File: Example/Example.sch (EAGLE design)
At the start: 20 parts, among them IC1 LM555D, IC2 74LS02D, IC3 74LS02D, J1 UX60-MB-5S8, SW1 MFS101D-6-Z

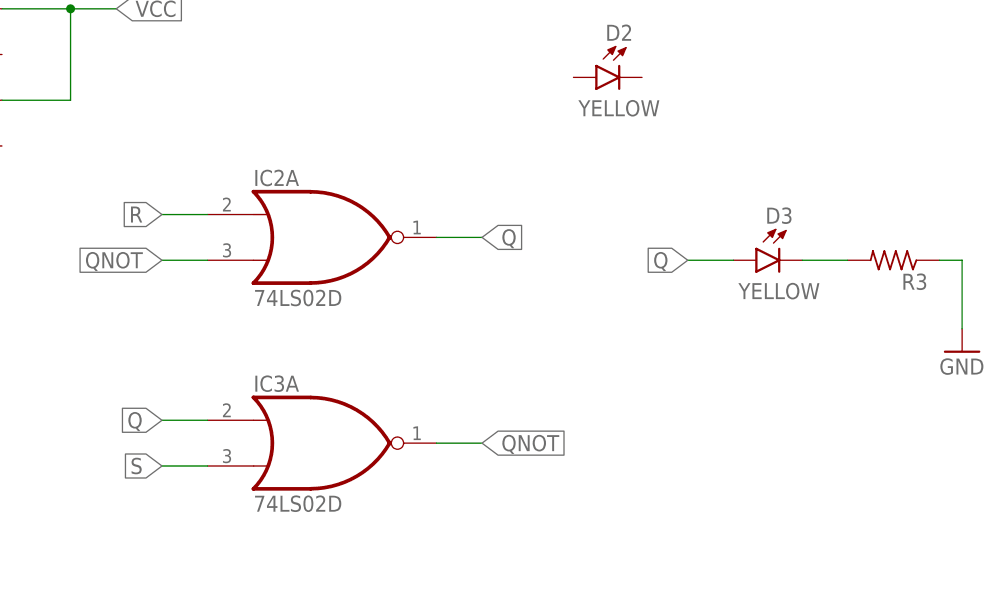
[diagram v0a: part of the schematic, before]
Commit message: Fixed issue of second NOR gate. However, did not delete second NOR gate.
I could not change the attributes of the NOR gates.
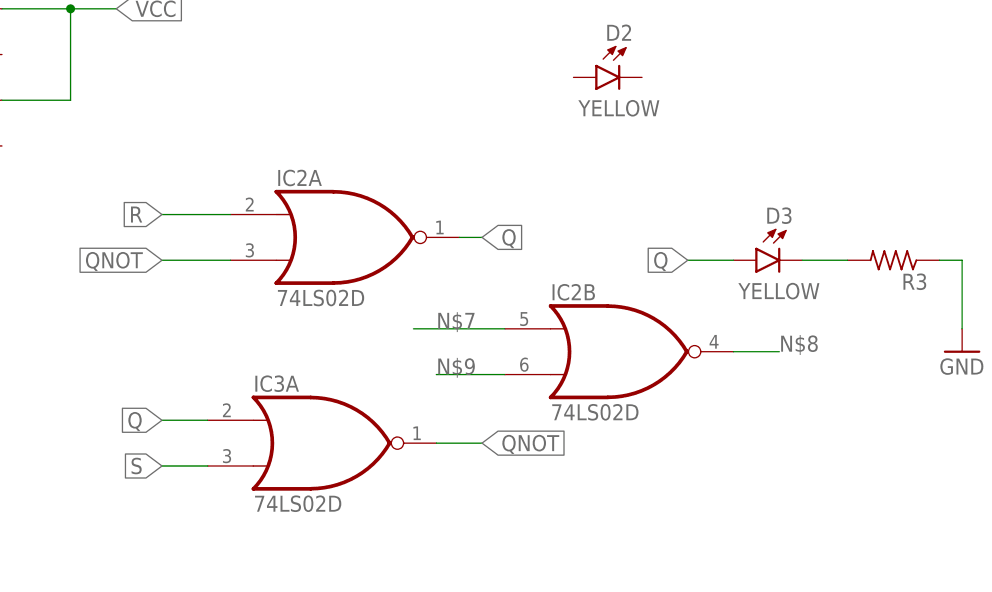
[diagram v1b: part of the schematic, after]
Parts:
- IC2: SPICEPREFIX (none) -> J
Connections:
- new net N$7: IC2B.I0
- new net N$8: IC2B.O
- new net N$9: IC2B.I1
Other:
- moved on the sheet: IC2A
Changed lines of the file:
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@@
 <?xml version="1.0" encoding="utf-8"?>
 <!DOCTYPE eagle SYSTEM "eagle.dtd">
-<eagle version="9.5.1">
+<eagle version="9.5.2">
 <drawing>
 <settings>
@@
 <part name="SUPPLY12" library="RoboJackets-Supplies" deviceset="GND" device=""/>
 <part name="SW1" library="Example" deviceset="MFS101D-6-Z" device="" override_package3d_urn="urn:adsk.eagle:package:25000897/2" override_package_urn="urn:adsk.eagle:footprint:25000899/1"/>
-<part name="IC2" library="74xx-us" library_urn="urn:adsk.eagle:library:88" deviceset="74*02" device="D" package3d_urn="urn:adsk.eagle:package:2917/1" technology="LS"/>
+<part name="IC2" library="74xx-us" library_urn="urn:adsk.eagle:library:88" deviceset="74*02" device="D" package3d_urn="urn:adsk.eagle:package:2917/1" technology="LS">
+<attribute name="SPICEPREFIX" value="J"/>
+</part>
 <part name="S1" library="adafruit" library_urn="urn:adsk.eagle:library:420" deviceset="40-XX" device="-ROUND" package3d_urn="urn:adsk.eagle:package:6240926/1"/>
 <part name="U$1" library="adafruit" library_urn="urn:adsk.eagle:library:420" deviceset="CR1220" device="SMT" package3d_urn="urn:adsk.eagle:package:6240665/1"/>
@@
 <attribute name="VALUE" x="107.696" y="154.178" size="1.778" layer="96" rot="R180"/>
 </instance>
-<instance part="IC2" gate="A" x="195.58" y="88.9" smashed="yes">
-<attribute name="NAME" x="187.96" y="94.615" size="1.778" layer="95"/>
-<attribute name="VALUE" x="187.96" y="81.28" size="1.778" layer="96"/>
+<instance part="IC2" gate="A" x="198.12" y="88.9" smashed="yes">
+<attribute name="NAME" x="190.5" y="94.615" size="1.778" layer="95"/>
+<attribute name="VALUE" x="190.5" y="81.28" size="1.778" layer="96"/>
 </instance>
 <instance part="S1" gate="1" x="127" y="88.9" smashed="yes" rot="R270">
@@
 <instance part="SUPPLY14" gate="G$1" x="144.78" y="93.98" smashed="yes">
 <attribute name="VALUE" x="142.24" y="91.44" size="1.778" layer="96"/>
+</instance>
+<instance part="IC2" gate="B" x="228.6" y="76.2" smashed="yes">
+<attribute name="NAME" x="220.98" y="81.915" size="1.778" layer="95"/>
+<attribute name="VALUE" x="220.98" y="68.58" size="1.778" layer="96"/>
 </instance>
 </instances>
@@
 <pinref part="IC2" gate="A" pin="I1"/>
 <label x="177.8" y="86.36" size="1.778" layer="95" rot="R180" xref="yes"/>
-<wire x1="182.88" y1="86.36" x2="177.8" y2="86.36" width="0.1524" layer="91"/>
+<wire x1="185.42" y1="86.36" x2="177.8" y2="86.36" width="0.1524" layer="91"/>
 </segment>
 <segment>
@@
 <pinref part="IC2" gate="A" pin="I0"/>
 <label x="177.8" y="91.44" size="1.778" layer="95" rot="R180" xref="yes"/>
-<wire x1="182.88" y1="91.44" x2="177.8" y2="91.44" width="0.1524" layer="91"/>
+<wire x1="185.42" y1="91.44" x2="177.8" y2="91.44" width="0.1524" layer="91"/>
 </segment>
 <segment>
@@
 <segment>
 <pinref part="IC2" gate="A" pin="O"/>
-<wire x1="208.28" y1="88.9" x2="213.36" y2="88.9" width="0.1524" layer="91"/>
+<wire x1="210.82" y1="88.9" x2="213.36" y2="88.9" width="0.1524" layer="91"/>
 <label x="213.36" y="88.9" size="1.778" layer="95" xref="yes"/>
 </segment>
@@
 </segment>
 </net>
+<net name="N$7" class="0">
+<segment>
+<pinref part="IC2" gate="B" pin="I0"/>
+<wire x1="215.9" y1="78.74" x2="205.74" y2="78.74" width="0.1524" layer="91"/>
+<label x="208.28" y="78.74" size="1.778" layer="95"/>
+</segment>
+</net>
+<net name="N$8" class="0">
+<segment>
+<pinref part="IC2" gate="B" pin="O"/>
+<wire x1="241.3" y1="76.2" x2="246.38" y2="76.2" width="0.1524" layer="91"/>
+<label x="246.38" y="76.2" size="1.778" layer="95"/>
+</segment>
+</net>
+<net name="N$9" class="0">
+<segment>
+<pinref part="IC2" gate="B" pin="I1"/>
+<wire x1="215.9" y1="73.66" x2="208.28" y2="73.66" width="0.1524" layer="91"/>
+<label x="208.28" y="73.66" size="1.778" layer="95"/>
+</segment>
+</net>

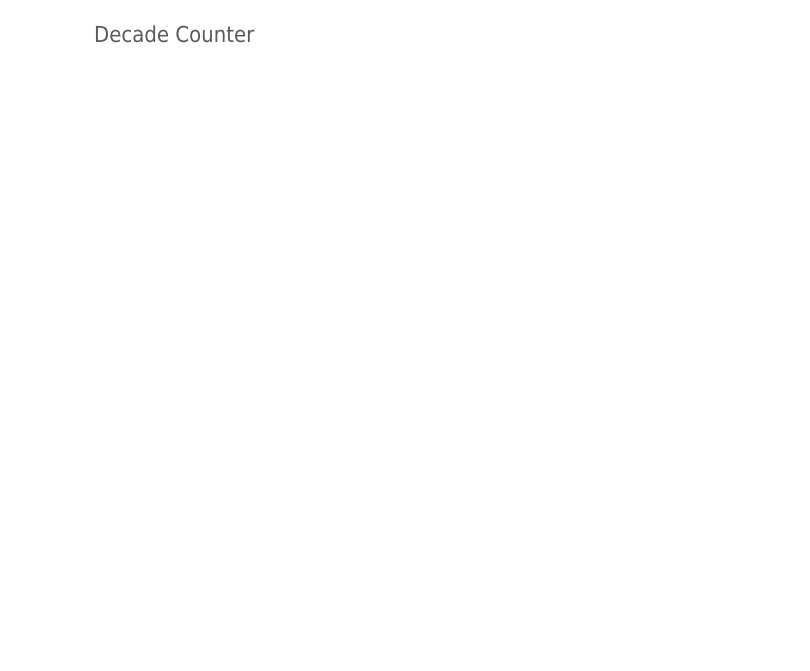
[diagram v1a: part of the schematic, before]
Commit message: Added CD4017 Decade Counter
Part can be found in the SparkFun-IC-Logiv Library
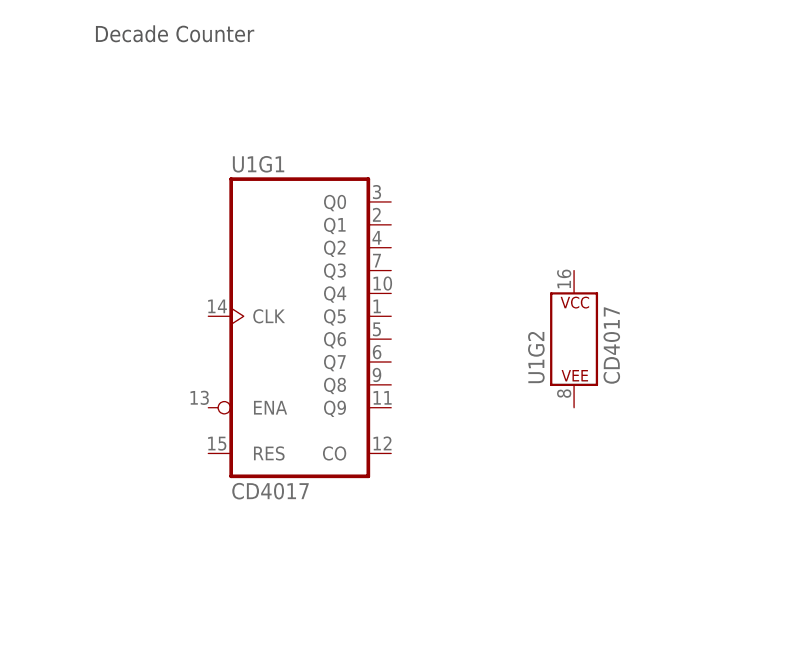
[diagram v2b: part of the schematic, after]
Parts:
- added U1: CD4017, SparkFun-IC-Logic:CD4017
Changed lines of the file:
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@@
 <part name="U$3" library="adafruit" library_urn="urn:adsk.eagle:library:420" deviceset="CR1220" device="SMT" package3d_urn="urn:adsk.eagle:package:6240665/1"/>
 <part name="SUPPLY14" library="RoboJackets-Supplies" deviceset="GND" device=""/>
+<part name="U1" library="SparkFun-IC-Logic" library_urn="urn:adsk.eagle:library:523" deviceset="CD4017" device="" package3d_urn="urn:adsk.eagle:package:38809/1" value="CD4017"/>
 </parts>
 <sheets>
@@
 <attribute name="VALUE" x="220.98" y="68.58" size="1.778" layer="96"/>
 </instance>
+<instance part="U1" gate="G1" x="175.26" y="170.18" smashed="yes">
+<attribute name="NAME" x="167.64" y="186.182" size="1.778" layer="95" font="vector"/>
+<attribute name="VALUE" x="167.64" y="149.86" size="1.778" layer="95" font="vector"/>
+</instance>
+<instance part="U1" gate="G2" x="205.74" y="167.64" smashed="yes">
+<attribute name="NAME" x="202.438" y="162.56" size="1.778" layer="95" font="vector" rot="R90"/>
+<attribute name="VALUE" x="210.82" y="162.56" size="1.778" layer="95" font="vector" rot="R90"/>
+</instance>
 </instances>

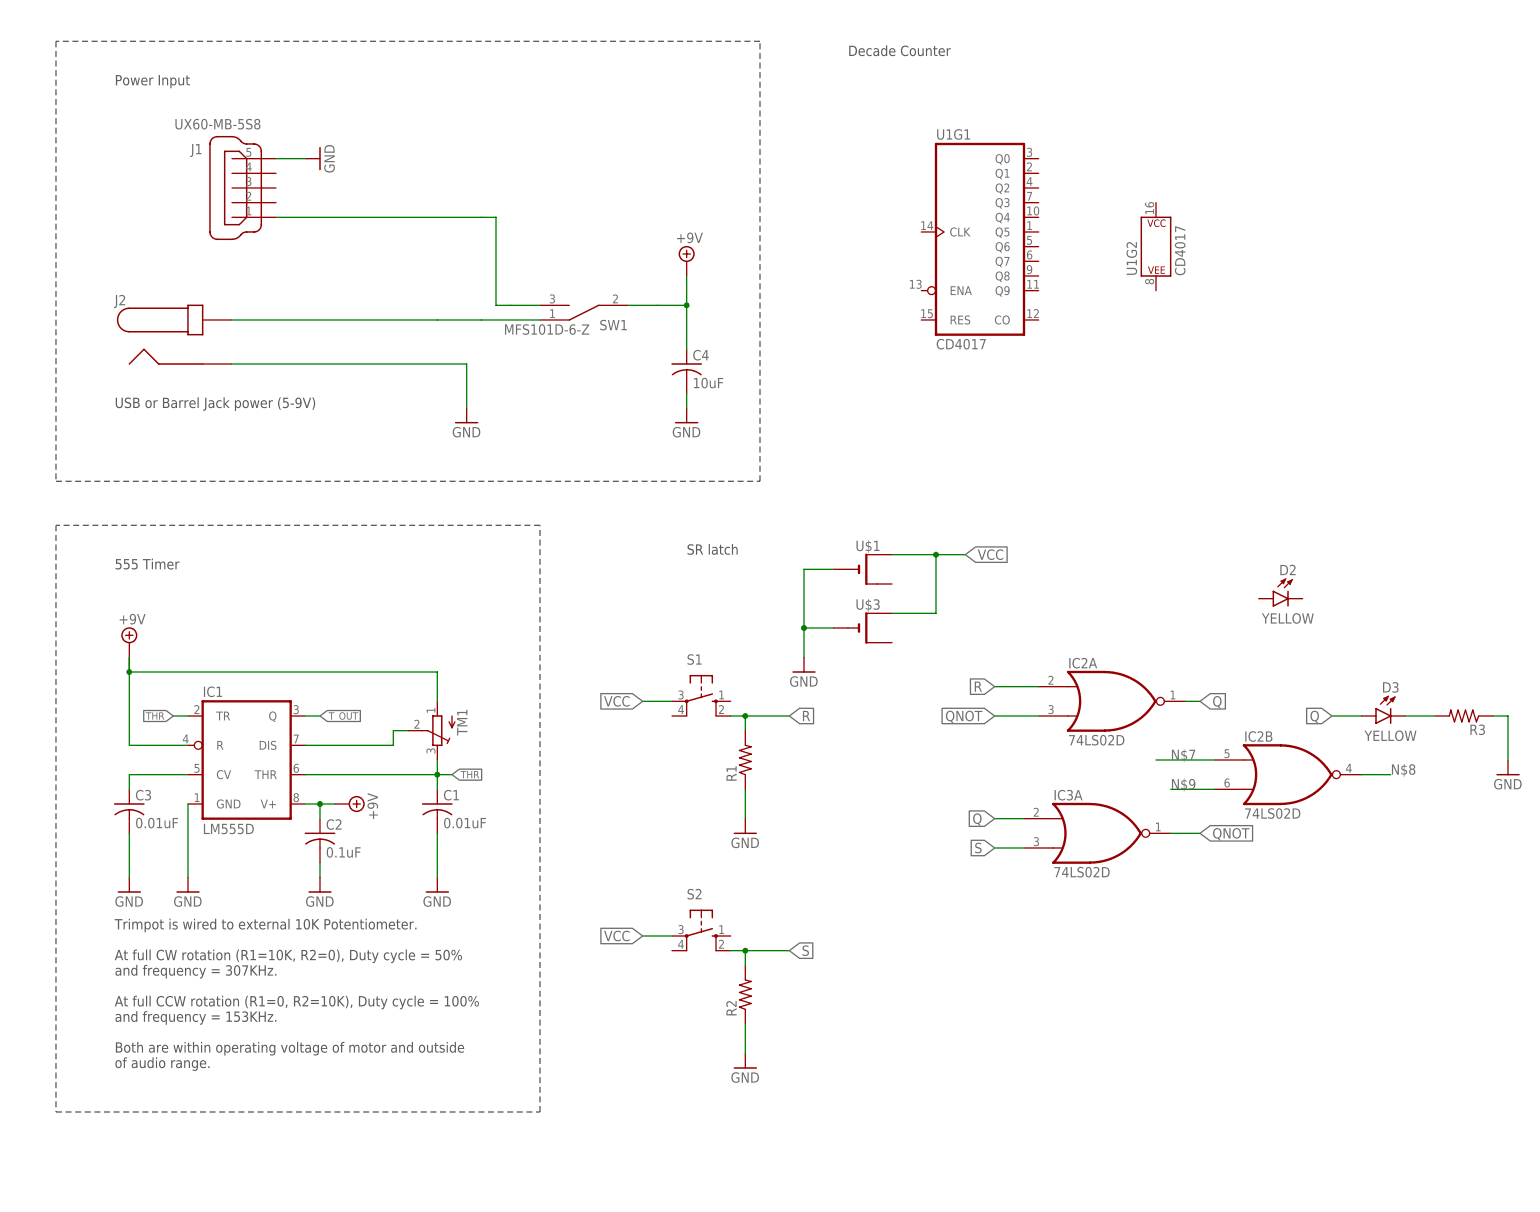
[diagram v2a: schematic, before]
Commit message: decade counter
leds for decade counter
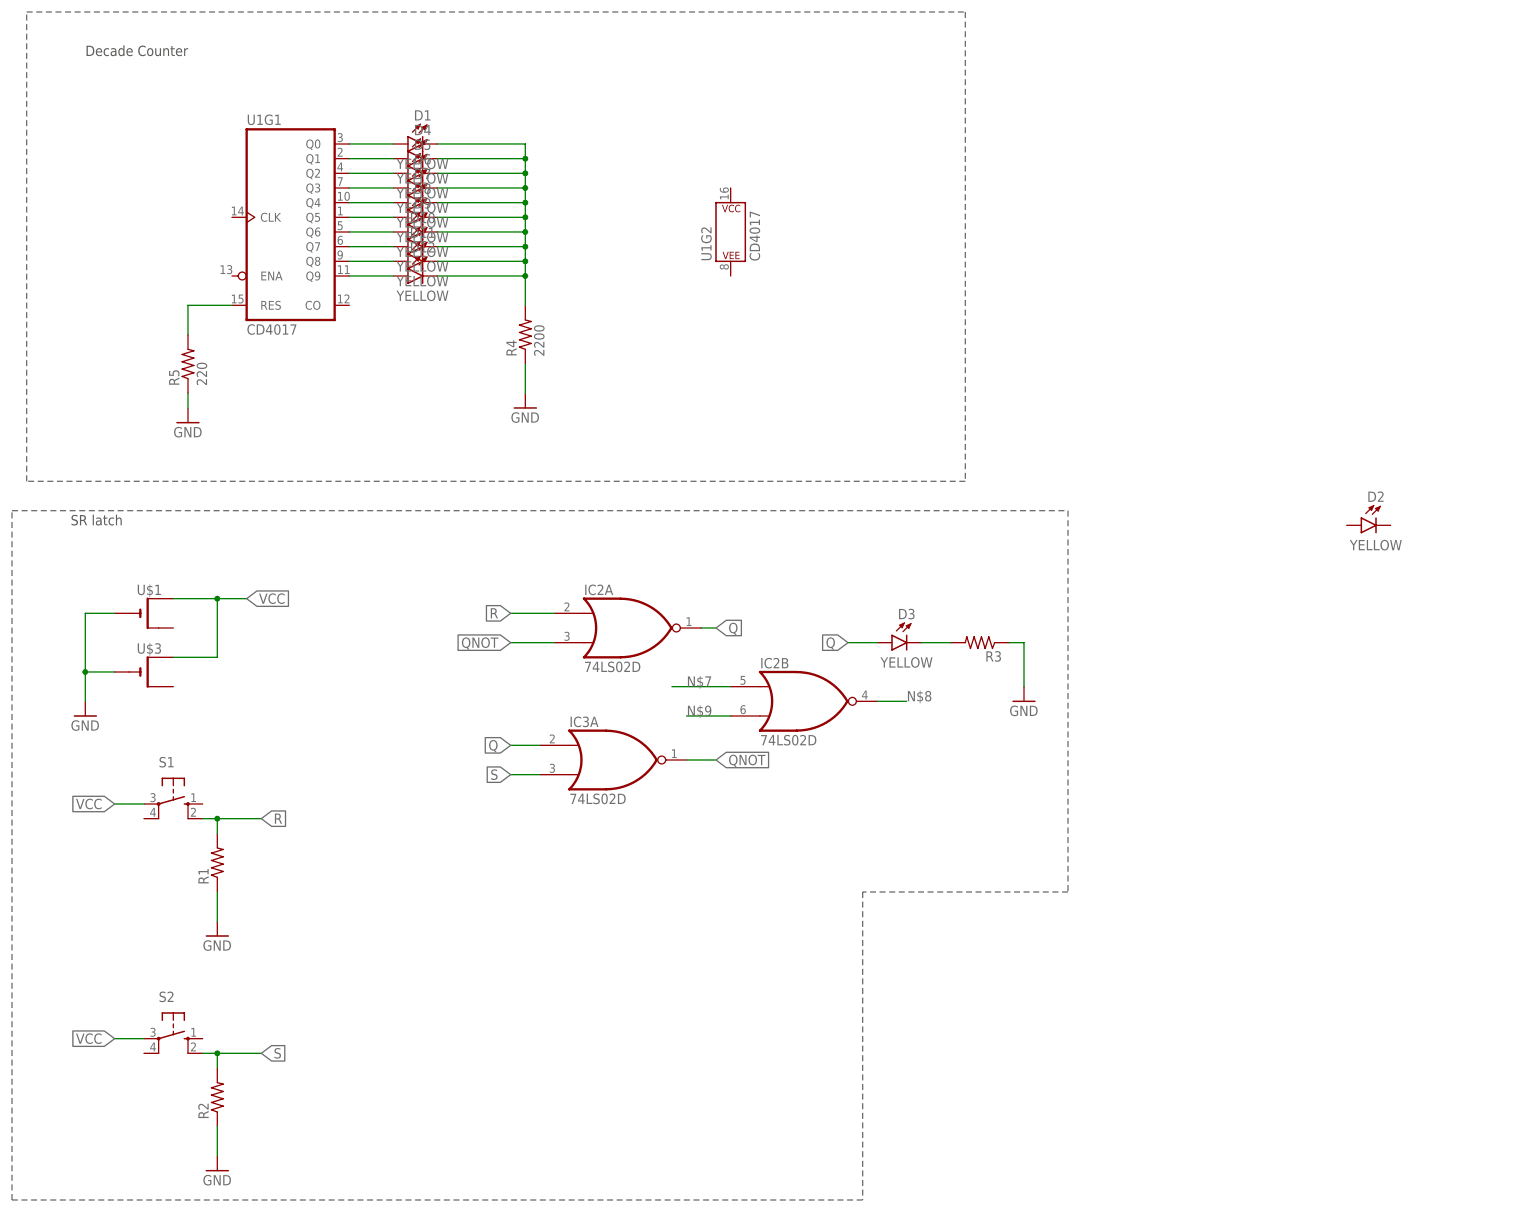
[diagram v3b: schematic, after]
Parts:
- removed C1, C3: 0.01uF, rcl:C-USC0603
- removed C2: 0.1uF, rcl:C-USC0603
- removed C4: 10uF, rcl:C-USC0603
- removed IC1: LM555D, adafruit:LM555D
- removed J1: UX60-MB-5S8, RoboJackets-Connectors:UX60-MB-5S8
- removed J2: (no value), RoboJackets-Connectors:PJ-037A
- removed SW1: MFS101D-6-Z, Example:MFS101D-6-Z
- removed TM1: (no value), adafruit:TRIMPOT3386
- added D1, D10, D11, D12, D4, D5, D6, D7, D8, D9: YELLOW, RoboJackets-LEDs:LED-SMD-YELLOW
- added R4: 2200, rcl:R-US_R0603
- added R5: 220, rcl:R-US_R0603
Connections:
- removed net +9V: C2.1, C4.1, IC1.R, IC1.V+, SW1.COMMON, TM1.A
- removed net N$1: IC1.DIS, TM1.S
- removed net N$3: C3.1, IC1.CV
- removed net N$4: J1.1, SW1.B
- removed net N$6: J2.1, SW1.A
- removed net THR: C1.1, IC1.THR, IC1.TR, TM1.E
- removed net T_OUT: IC1.Q
- new net N$10: D1.A, U1G1.Q0
- new net N$11: D4.A, U1G1.Q1
- new net N$12: D5.A, U1G1.Q2
- new net N$13: D6.A, U1G1.Q3
- new net N$14: D7.A, U1G1.Q4
- new net N$15: D8.A, U1G1.Q5
- new net N$16: D9.A, U1G1.Q6
- new net N$17: D10.A, U1G1.Q7
- new net N$18: D11.A, U1G1.Q8
- new net N$19: D12.A, U1G1.Q9
- new net N$20: D1.C, D10.C, D11.C, D12.C, D4.C, D5.C, D6.C, D7.C, D8.C, D9.C, R4.2
- new net N$21: R5.2, U1G1.RES
- net GND: now also R4.1, R5.1; no longer C1.2, C2.2, C3.2, C4.2, IC1.GND, J1.5, J2.2
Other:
- note removed: "555 Timer"
- note removed: "Power Input"
- note removed: "Trimpot is wired to external 10K Potentiometer. At full CW rotation (R1=10K, R2=0), Duty cycle = 50% and frequency = 307KHz. At full CCW rotation (R1=0, R2=10K), Duty cycle = 100% and frequency = 153KHz. Both are within operating voltage of motor and outside of audio range."
- note removed: "USB or Barrel Jack power (5-9V)"
- moved on the sheet: D2, D3, IC2A, IC2B, IC3A, R1, R2, R3, S1, S2, U$1, U$3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
